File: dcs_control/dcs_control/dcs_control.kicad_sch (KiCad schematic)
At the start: 9 parts, among them SW1 RotaryEncoder_Switch, SW2 RotaryEncoder_Switch, SW3 RotaryEncoder_Switch, SW4 SW_SPDT_MSM, SW5 SW_SPDT_MSM, SW6 SW_SPDT_MSM, SW7 SW_SPDT_MSM, SW8 SW_Push, U1 Sparkfun_Pro_Micro

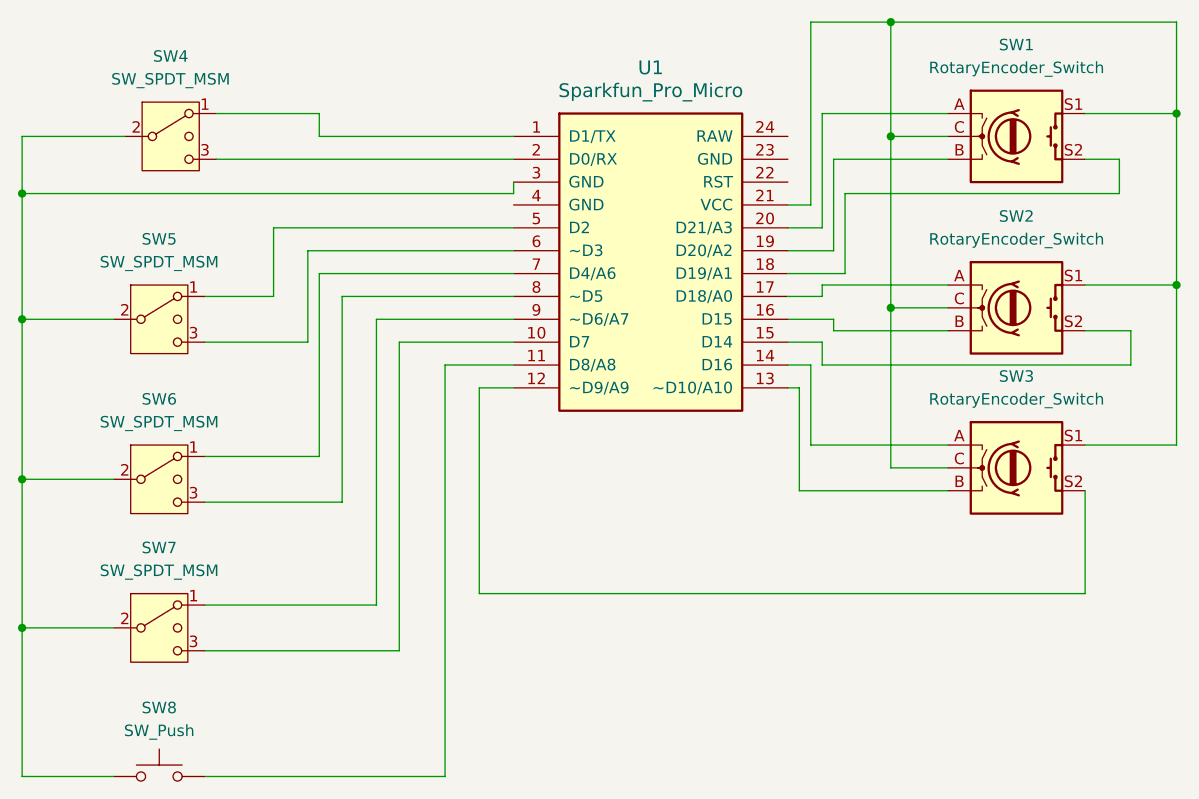
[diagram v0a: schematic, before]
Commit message: DcsControl: Schematics update
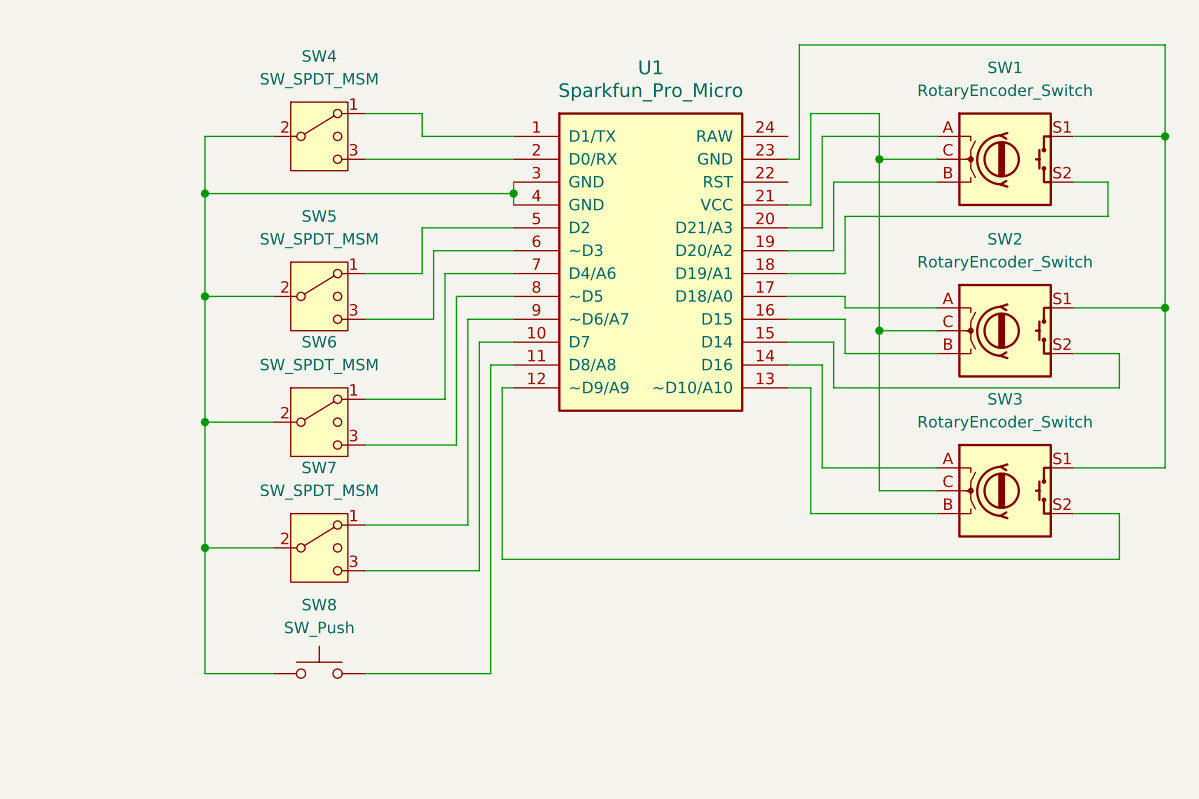
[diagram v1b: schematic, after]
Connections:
- net at SW4.2 (3), SW5.2 (3), SW6.2 (3)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: now also U1.4 (GND)
- net at SW1.C, SW2.C, SW3.C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: no longer SW1.S1, SW2.S1, SW3.S1
- net at U1.23 (GND): now also SW1.S1, SW2.S1, SW3.S1
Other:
- moved on the sheet: SW1, SW2, SW3, SW4, SW5, SW6, SW7, SW8
